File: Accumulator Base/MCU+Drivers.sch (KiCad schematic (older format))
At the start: 30 parts, among them Q10 Q_NMOS_DGS, Q11 Q_NMOS_DGS, Q12 Q_NMOS_DGS, Q13 Q_NMOS_DGS, Q14 Q_NMOS_DGS, Q15 Q_NMOS_DGS, Q16 Q_NMOS_DGS, Q17 Q_NMOS_DGS, Q18 Q_NMOS_DGS, Q19 Q_NMOS_DGS, Q20 Q_NMOS_DGS, Q21 Q_NMOS_DGS, U4 LAUNCHXL-F28379D

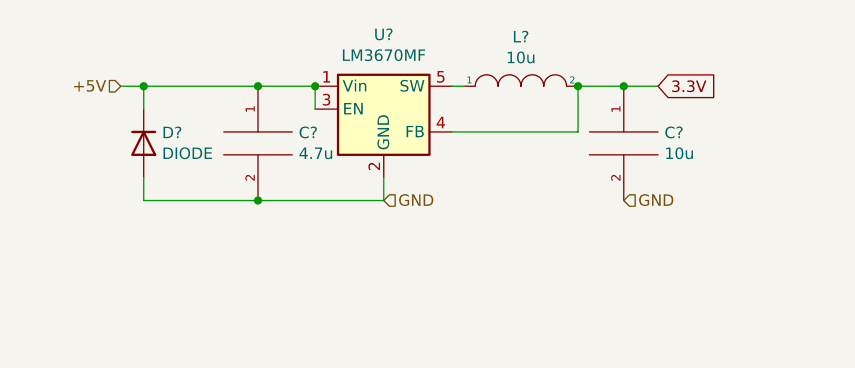
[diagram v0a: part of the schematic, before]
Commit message: Energy meter LV power connector added to Accumulator Base schematic
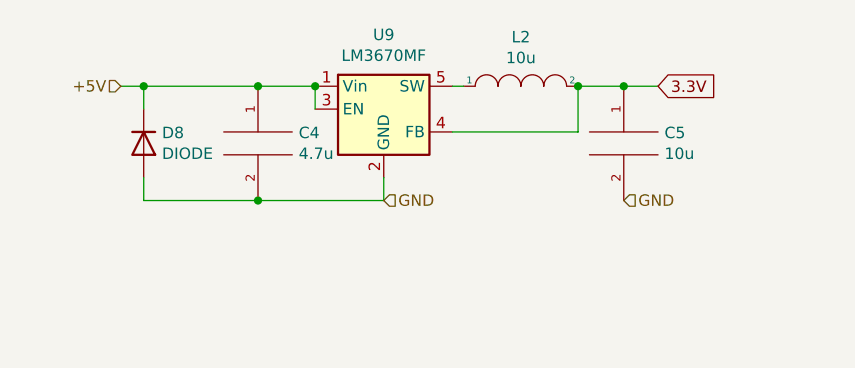
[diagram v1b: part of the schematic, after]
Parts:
- gave numbers to parts that had none: 5
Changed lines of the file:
@@
 Reset
 $Comp
-L Regulator_Switching:LM3670MF U?
+L Regulator_Switching:LM3670MF U9
 U 1 1 5F3DD55E
 P 4700 1050
-F 0 "U?" H 4700 1375 50  0000 C CNN
+F 0 "U9" H 4700 1375 50  0000 C CNN
 F 1 "LM3670MF" H 4700 1284 50  0000 C CNN
 F 2 "Package_TO_SOT_SMD:TSOT-23-5" H 4750 800 50  0001 L CNN
@@
 Connection ~ 4400 950
 $Comp
-L pspice:C C?
+L pspice:C C4
 U 1 1 5F3DF85E
 P 4150 1200
-F 0 "C?" H 4328 1246 50  0000 L CNN
+F 0 "C4" H 4328 1246 50  0000 L CNN
 F 1 "4.7u" H 4328 1155 50  0000 L CNN
 F 2 "" H 4150 1200 50  0001 C CNN
@@
 	4150 1450 4700 1450
 $Comp
-L pspice:INDUCTOR L?
+L pspice:INDUCTOR L2
 U 1 1 5F3E1A46
 P 5300 950
-F 0 "L?" H 5300 1165 50  0000 C CNN
+F 0 "L2" H 5300 1165 50  0000 C CNN
 F 1 "10u" H 5300 1074 50  0000 C CNN
 F 2 "" H 5300 950 50  0001 C CNN
@@
 Connection ~ 5550 950
 $Comp
-L pspice:C C?
+L pspice:C C5
 U 1 1 5F3E3756
 P 5750 1200
-F 0 "C?" H 5928 1246 50  0000 L CNN
+F 0 "C5" H 5928 1246 50  0000 L CNN
 F 1 "10u" H 5928 1155 50  0000 L CNN
 F 2 "" H 5750 1200 50  0001 C CNN
@@
 3.3V
 $Comp
-L Simulation_SPICE:DIODE D?
+L Simulation_SPICE:DIODE D8
 U 1 1 5F3E4BB6
 P 3650 1200
-F 0 "D?" V 3696 1120 50  0000 R CNN
+F 0 "D8" V 3696 1120 50  0000 R CNN
 F 1 "DIODE" V 3605 1120 50  0000 R CNN
 F 2 "" H 3650 1200 50  0001 C CNN

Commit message: Accumulator Base layout with no traces
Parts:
- added Q5: Q_NMOS_GDS, Package_TO_SOT_SMD:SOT-223-3_TabPin2, symbol Device:Q_NMOS_GDS
- added R17: 10k, Resistor_SMD:R_1206_3216Metric, symbol Device:R
- C4, C5: footprint (none) -> Capacitor_SMD:C_0805_2012Metric
- D8: footprint (none) -> Diode_SMD:D_SOD-323
- L2: footprint (none) -> Inductor_SMD:L_1210_3225Metric
- Q10, Q11, Q12, Q13, Q14, Q15, Q16, Q17, Q18, Q19, Q20, Q21: value Q_NMOS_DGS -> Q_NMOS_GDS; footprint Package_TO_SOT_THT:TO-220-3_Horizontal_TabDown -> Package_TO_SOT_SMD:SOT-223-3_TabPin2; symbol Device:Q_NMOS_DGS -> Device:Q_NMOS_GDS
- R18, R19, R20, R21, R22, R23, R24, R25, R26, R27, R28, R29: footprint (none) -> Resistor_SMD:R_1206_3216Metric
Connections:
- net HVD_InvInterlock is gone; now on net 3.3V: Q20.2 (D)
- net InvInterlock_TSMP is gone; now on net 3.3V: Q13.2 (D)
- net TSMP_Charger is gone; now on net 3.3V: Q12.2 (D)
- net +5V: now also U4.118; no longer Q10.1 (D), Q11.1 (D), Q12.1 (D), Q13.1 (D), Q14.1 (D), Q15.1 (D), Q16.1 (D), Q17.1 (D), Q18.1 (D), Q19.1 (D), Q20.1 (D), Q21.1 (D)
- net 3.3V: now also Q10.2 (D), Q11.2 (D), Q14.2 (D), Q15.2 (D), Q16.2 (D), Q17.2 (D), Q18.2 (D), Q19.2 (D), Q21.2 (D), U4.2, Q5.2 (D)
- net AIR+-welded-closed: now also Q18.1 (G); no longer Q18.2 (G)
- net AIR--welded-closed: now also Q19.1 (G); no longer Q19.2 (G)
- net Discharge: now also Q15.1 (G); no longer Q15.2 (G)
- net GND: now also U4.116, R17.2
- net IMD-output: now also Q17.1 (G); no longer Q17.2 (G)
- net Precharge: now also Q14.1 (G); no longer Q14.2 (G)
- net SDC_out: now also Q21.1 (G); no longer Q21.2 (G)
- net Safe_in: now also Q10.1 (G); no longer Q10.2 (G)
- net Safe_out: now also Q11.1 (G); no longer Q11.2 (G)
- net TS_Ready: now also Q16.1 (G); no longer Q16.2 (G)
- net RTD: now reaches U4.17
- net Reg_EN: now reaches U4.18
- net DCDC_EN: now reaches U4.89
- net DCDC_EN: now also Q5.3 (S), R17.1
- new net Charger_TSMP: Q13.1 (G)
- new net DCDC_ON: Q5.1 (G)
- new net HVD_Charger: Q20.1 (G)
- new net TSMP_Inv: Q12.1 (G)
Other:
- note added: "Coil model: TFM322512ALMA100MTAA"

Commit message: Libraries added to project folders
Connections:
- net RTD renamed RTD_accu
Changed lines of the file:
@@
 $Descr A4 11693 8268
 encoding utf-8
-Sheet 3 4
+Sheet 4 4
 Title ""
 Date ""
@@
 Text Notes 4750 650  0    50   ~ 0
 Coil model: TFM322512ALMA100MTAA
-Text HLabel 5950 2600 1    50   Input ~ 0
-RTD
-Text HLabel 5850 2600 1    50   Input ~ 0
-Reg_EN
 Text GLabel 4200 2600 1    50   Input ~ 0
 3.3V
@@
 Text HLabel 6350 4750 3    50   Input ~ 0
 GND
+Text HLabel 5950 2600 1    50   Input ~ 0
+RTD_accu
+Text HLabel 5850 2600 1    50   Input ~ 0
+Reg_EN
 $EndSCHEMATC

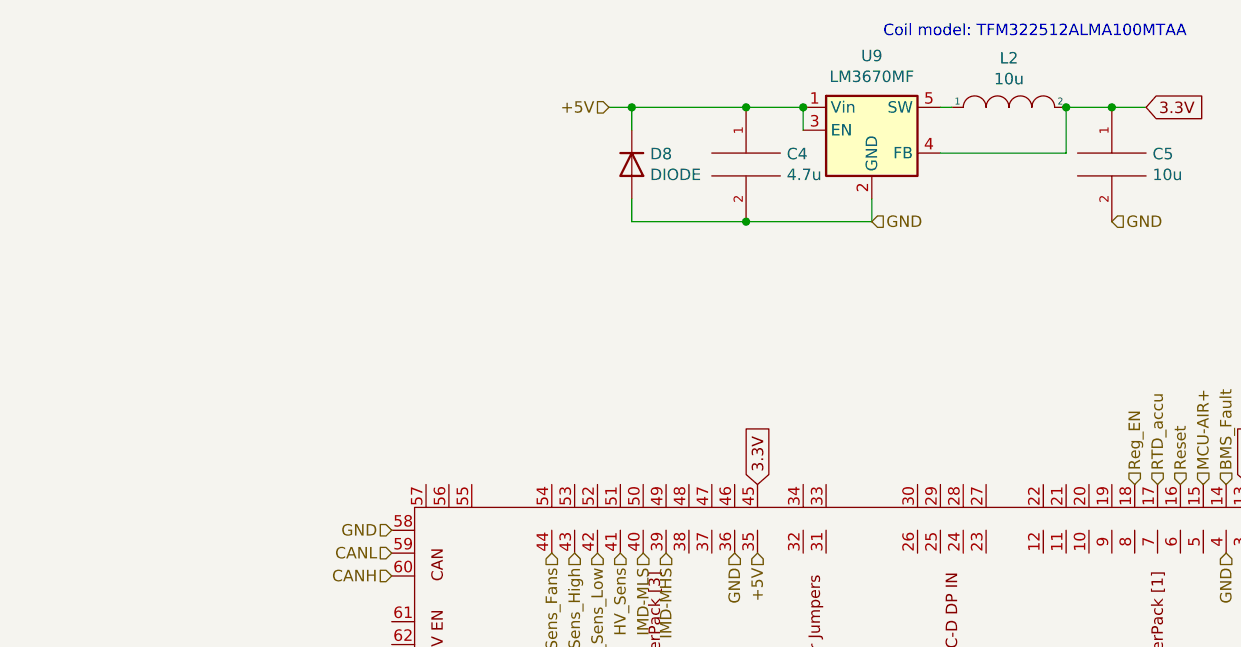
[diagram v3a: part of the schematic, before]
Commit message: Changed right angle connectors to straight ones and added LCD and EM connectors
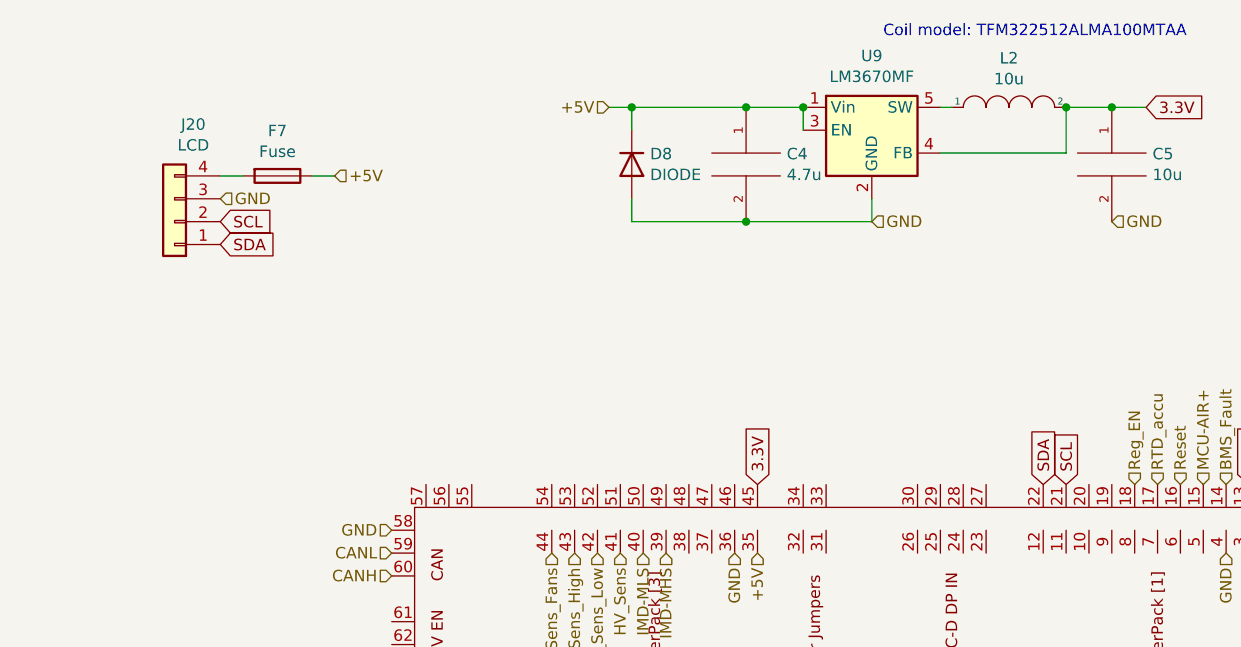
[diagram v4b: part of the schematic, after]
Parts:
- added F7: Fuse, Fuse:Fuse_1206_3216Metric, symbol Device:Fuse
- added J20: LCD, Connector_Molex:Molex_Micro-Fit_3.0_43650-0415_1x04_P3.00mm_Vertical, symbol Connector_Generic:Conn_01x04
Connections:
- net +5V: now also F7.1
- net GND: now also J20.3 (Pin_3)
- net SCL: now reaches U4.21
- net SCL: now also J20.2 (Pin_2)
- net SDA: now reaches U4.22
- net SDA: now also J20.1 (Pin_1)
- new net: F7.2, J20.4 (Pin_4)
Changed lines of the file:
@@
 Text HLabel 5850 2600 1    50   Input ~ 0
 Reg_EN
+$Comp
+L Connector_Generic:Conn_01x04 J20
+U 1 1 5F3F29A1
+P 1650 1450
+F 0 "J20" H 1568 1025 50  0000 C CNN
+F 1 "LCD" H 1568 1116 50  0000 C CNN
+F 2 "Connector_Molex:Molex_Micro-Fit_3.0_43650-0415_1x04_P3.00mm_Vertical" H 1650 1450 50  0001 C CNN
+F 3 "~" H 1650 1450 50  0001 C CNN
+	1    1650 1450
+	-1   0    0    1
+$EndComp
+Text HLabel 2350 1250 2    50   Input ~ 0
++5V
+Text HLabel 1850 1350 2    50   Input ~ 0
+GND
+Text GLabel 1850 1450 2    50   Input ~ 0
+SCL
+Text GLabel 1850 1550 2    50   Input ~ 0
+SDA
+Text GLabel 5450 2600 1    50   Input ~ 0
+SDA
+Text GLabel 5550 2600 1    50   Input ~ 0
+SCL
+$Comp
+L Device:Fuse F7
+U 1 1 5F3FA253
+P 2100 1250
+F 0 "F7" V 1903 1250 50  0000 C CNN
+F 1 "Fuse" V 1994 1250 50  0000 C CNN
+F 2 "Fuse:Fuse_1206_3216Metric" V 2030 1250 50  0001 C CNN
+F 3 "~" H 2100 1250 50  0001 C CNN
+	1    2100 1250
+	0    1    1    0
+$EndComp
+Wire Wire Line
+	1850 1250 1950 1250
+Wire Wire Line
+	2250 1250 2350 1250
 $EndSCHEMATC

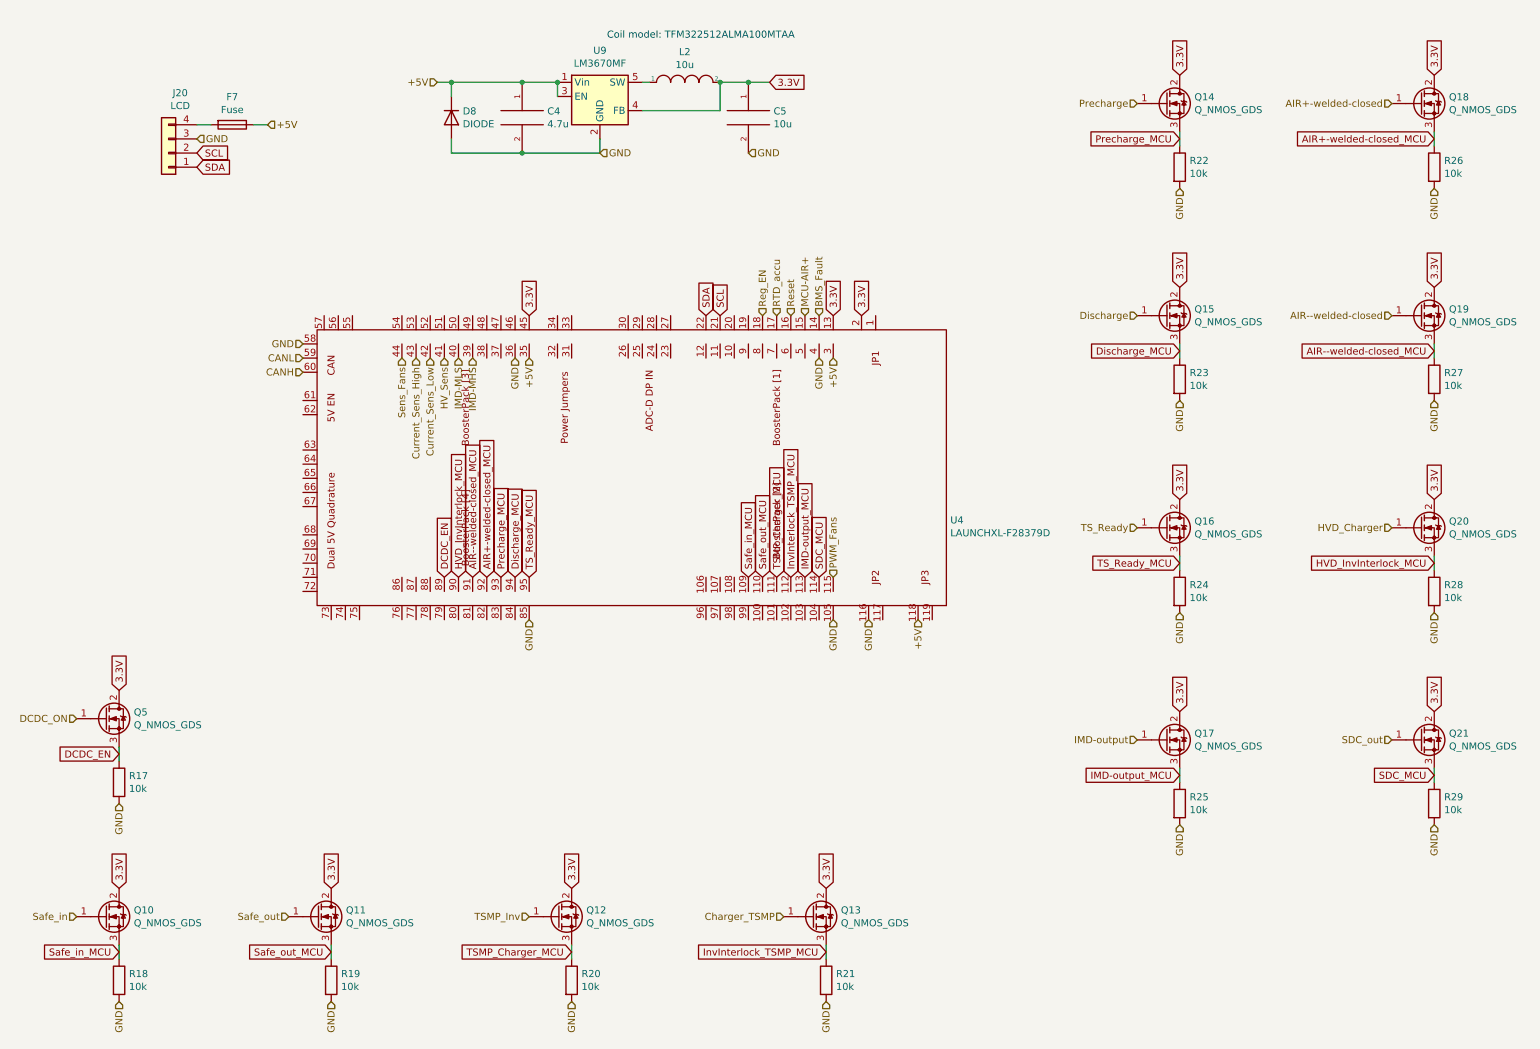
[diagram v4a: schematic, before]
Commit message: fp-lib-table files unignored and pull-down resistors added on NMOS gates in Base PCB
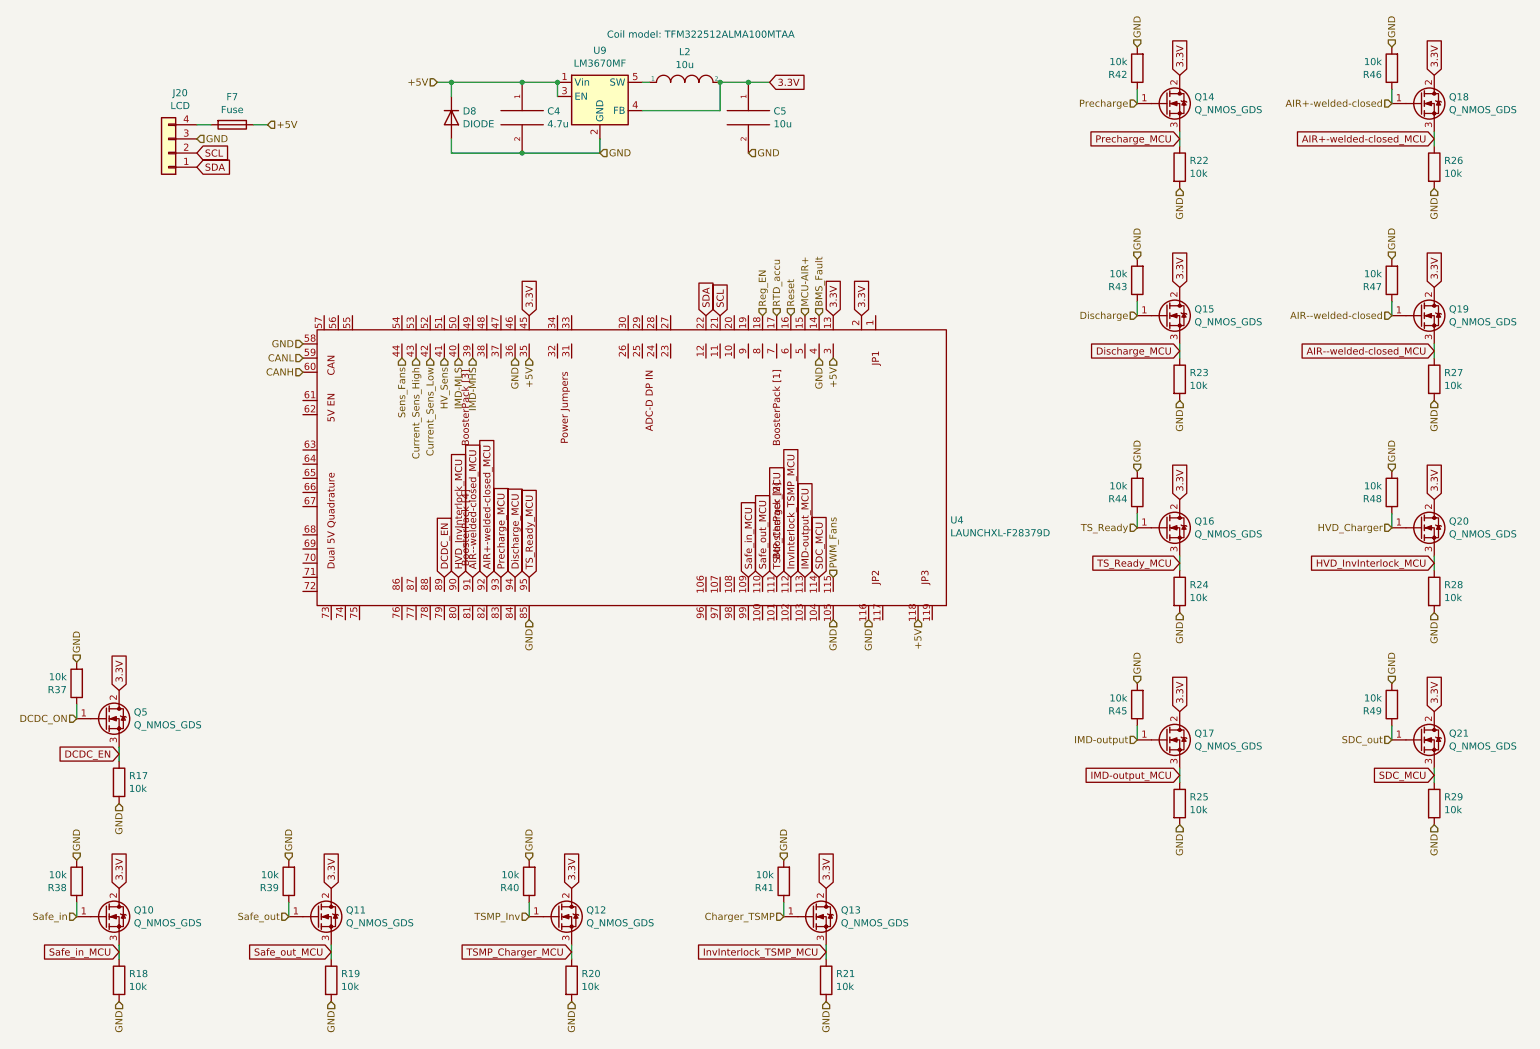
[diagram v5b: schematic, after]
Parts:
- added R37, R38, R39, R40, R41, R42, R43, R44, R45, R46, R47, R48, R49: 10k, Resistor_SMD:R_1206_3216Metric, symbol Device:R
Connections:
- net AIR+-welded-closed: now also R46.1
- net AIR--welded-closed: now also R47.1
- net Charger_TSMP: now also R41.1
- net DCDC_ON: now also R37.1
- net Discharge: now also R43.1
- net GND: now also R37.2, R38.2, R39.2, R40.2, R41.2, R42.2, R43.2, R44.2, R45.2, R46.2, R47.2, R48.2, R49.2
- net HVD_Charger: now also R48.1
- net IMD-output: now also R45.1
- net Precharge: now also R42.1
- net SDC_out: now also R49.1
- net Safe_in: now also R38.1
- net Safe_out: now also R39.1
- net TSMP_Inv: now also R40.1
- net TS_Ready: now also R44.1
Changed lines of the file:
@@
 Wire Wire Line
 	2250 1250 2350 1250
+$Comp
+L Device:R R37
+U 1 1 5F475781
+P 1000 5200
+F 0 "R37" H 1070 5246 50  0000 L CNN
+F 1 "10k" H 1070 5155 50  0000 L CNN
+F 2 "Resistor_SMD:R_1206_3216Metric" V 930 5200 50  0001 C CNN
+F 3 "~" H 1000 5200 50  0001 C CNN
+	1    1000 5200
+	-1   0    0    1
+$EndComp
+Text HLabel 1000 5050 1    50   Input ~ 0
+GND
+Wire Wire Line
+	1000 5350 1000 5450
+$Comp
+L Device:R R38
+U 1 1 5F4786AC
+P 1000 6600
+F 0 "R38" H 1070 6646 50  0000 L CNN
+F 1 "10k" H 1070 6555 50  0000 L CNN
+F 2 "Resistor_SMD:R_1206_3216Metric" V 930 6600 50  0001 C CNN
+F 3 "~" H 1000 6600 50  0001 C CNN
+	1    1000 6600
+	-1   0    0    1
+$EndComp
+Text HLabel 1000 6450 1    50   Input ~ 0
+GND
+Wire Wire Line
+	1000 6750 1000 6850
+$Comp
+L Device:R R39
+U 1 1 5F4799F5
+P 2500 6600
+F 0 "R39" H 2570 6646 50  0000 L CNN
+F 1 "10k" H 2570 6555 50  0000 L CNN
+F 2 "Resistor_SMD:R_1206_3216Metric" V 2430 6600 50  0001 C CNN
+F 3 "~" H 2500 6600 50  0001 C CNN
+	1    2500 6600
+	-1   0    0    1
+$EndComp
+Text HLabel 2500 6450 1    50   Input ~ 0
+GND
+Wire Wire Line
+	2500 6750 2500 6850
+$Comp
+L Device:R R40
+U 1 1 5F47AD81
+P 4200 6600
+F 0 "R40" H 4270 6646 50  0000 L CNN
+F 1 "10k" H 4270 6555 50  0000 L CNN
+F 2 "Resistor_SMD:R_1206_3216Metric" V 4130 6600 50  0001 C CNN
+F 3 "~" H 4200 6600 50  0001 C CNN
+	1    4200 6600
+	-1   0    0    1
+$EndComp
+Text HLabel 4200 6450 1    50   Input ~ 0
+GND
+Wire Wire Line
+	4200 6750 4200 6850
+$Comp
+L Device:R R41
+U 1 1 5F47BD71
+P 6000 6600
+F 0 "R41" H 6070 6646 50  0000 L CNN
+F 1 "10k" H 6070 6555 50  0000 L CNN
+F 2 "Resistor_SMD:R_1206_3216Metric" V 5930 6600 50  0001 C CNN
+F 3 "~" H 6000 6600 50  0001 C CNN
+	1    6000 6600
+	-1   0    0    1
+$EndComp
+Text HLabel 6000 6450 1    50   Input ~ 0
+GND
+Wire Wire Line
+	6000 6750 6000 6850
+$Comp
+L Device:R R45
+U 1 1 5F47D7B0
+P 8500 5350
+F 0 "R45" H 8570 5396 50  0000 L CNN
+F 1 "10k" H 8570 5305 50  0000 L CNN
+F 2 "Resistor_SMD:R_1206_3216Metric" V 8430 5350 50  0001 C CNN
+F 3 "~" H 8500 5350 50  0001 C CNN
+	1    8500 5350
+	-1   0    0    1
+$EndComp
+Text HLabel 8500 5200 1    50   Input ~ 0
+GND
+Wire Wire Line
+	8500 5500 8500 5600
+$Comp
+L Device:R R49
+U 1 1 5F47E78C
+P 10300 5350
+F 0 "R49" H 10370 5396 50  0000 L CNN
+F 1 "10k" H 10370 5305 50  0000 L CNN
+F 2 "Resistor_SMD:R_1206_3216Metric" V 10230 5350 50  0001 C CNN
+F 3 "~" H 10300 5350 50  0001 C CNN
+	1    10300 5350
+	-1   0    0    1
+$EndComp
+Text HLabel 10300 5200 1    50   Input ~ 0
+GND
+Wire Wire Line
+	10300 5500 10300 5600
+$Comp
+L Device:R R44
+U 1 1 5F480036
+P 8500 3850
+F 0 "R44" H 8570 3896 50  0000 L CNN
+F 1 "10k" H 8570 3805 50  0000 L CNN
+F 2 "Resistor_SMD:R_1206_3216Metric" V 8430 3850 50  0001 C CNN
+F 3 "~" H 8500 3850 50  0001 C CNN
+	1    8500 3850
+	-1   0    0    1
+$EndComp
+Text HLabel 8500 3700 1    50   Input ~ 0
+GND
+Wire Wire Line
+	8500 4000 8500 4100
+$Comp
+L Device:R R48
+U 1 1 5F4816B5
+P 10300 3850
+F 0 "R48" H 10370 3896 50  0000 L CNN
+F 1 "10k" H 10370 3805 50  0000 L CNN
+F 2 "Resistor_SMD:R_1206_3216Metric" V 10230 3850 50  0001 C CNN
+F 3 "~" H 10300 3850 50  0001 C CNN
+	1    10300 3850
+	-1   0    0    1
+$EndComp
+Text HLabel 10300 3700 1    50   Input ~ 0
+GND
+Wire Wire Line
+	10300 4000 10300 4100
+$Comp
+L Device:R R43
+U 1 1 5F48294F
+P 8500 2350
+F 0 "R43" H 8570 2396 50  0000 L CNN
+F 1 "10k" H 8570 2305 50  0000 L CNN
+F 2 "Resistor_SMD:R_1206_3216Metric" V 8430 2350 50  0001 C CNN
+F 3 "~" H 8500 2350 50  0001 C CNN
+	1    8500 2350
+	-1   0    0    1
+$EndComp
+Text HLabel 8500 2200 1    50   Input ~ 0
+GND
+Wire Wire Line
+	8500 2500 8500 2600
+$Comp
+L Device:R R47
+U 1 1 5F484490
+P 10300 2350
+F 0 "R47" H 10370 2396 50  0000 L CNN
+F 1 "10k" H 10370 2305 50  0000 L CNN
+F 2 "Resistor_SMD:R_1206_3216Metric" V 10230 2350 50  0001 C CNN
+F 3 "~" H 10300 2350 50  0001 C CNN
+	1    10300 2350
+	-1   0    0    1
+$EndComp
+Text HLabel 10300 2200 1    50   Input ~ 0
+GND
+Wire Wire Line
+	10300 2500 10300 2600
+$Comp
+L Device:R R42
+U 1 1 5F4858DB
+P 8500 850
+F 0 "R42" H 8570 896 50  0000 L CNN
+F 1 "10k" H 8570 805 50  0000 L CNN
+F 2 "Resistor_SMD:R_1206_3216Metric" V 8430 850 50  0001 C CNN
+F 3 "~" H 8500 850 50  0001 C CNN
+	1    8500 850
+	-1   0    0    1
+$EndComp
+Text HLabel 8500 700  1    50   Input ~ 0
+GND
+Wire Wire Line
+	8500 1000 8500 1100
+$Comp
+L Device:R R46
+U 1 1 5F4870FE
+P 10300 850
+F 0 "R46" H 10370 896 50  0000 L CNN
+F 1 "10k" H 10370 805 50  0000 L CNN
+F 2 "Resistor_SMD:R_1206_3216Metric" V 10230 850 50  0001 C CNN
+F 3 "~" H 10300 850 50  0001 C CNN
+	1    10300 850
+	-1   0    0    1
+$EndComp
+Text HLabel 10300 700  1    50   Input ~ 0
+GND
+Wire Wire Line
+	10300 1000 10300 1100
 $EndSCHEMATC
